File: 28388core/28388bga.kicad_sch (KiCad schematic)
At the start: 132 parts, among them IC1 F28388DZWTS, IC2 TPS62420DRCT, IC6 OPA4350EA_250, IC7 TPS3702CX33DDCT, IC8 CDCLVC1104PW, IC9 TPS3702CX12DDCT, J9 Conn_02x07_Odd_Even, Q1 FMMT618TA, Q11 AT24C16C-SSHM-T, Q2 FMMT618TA, Q4 FMMT618TA, Q46 TYPEC-304-ACP16, Q7 FMMT618TA, SW1 SW_DIP_x02, SW2 SW_Push, U1 ADR423ARMZ, Y1 ECS-2520S33-250-FN-TR

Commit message: 使用4个50PIN引脚，通常按照337封装分配位置
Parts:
- removed CN4: ~, 1mmlab_footprint:CONN-SMD_200P-P0.50_X0510WVS-200AS-LPV01, symbol 1mmlab:X0510WVS-200AS-LPV01
- added J2, J3, J4, J5: ~, 1mmlab_footprint:CONN-SMD_50P-P0.50_XKB_X0515WVS-50AS-9TV01, symbol 1mmlab:X0515WVS-50AS-9TV01
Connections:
- net GPIO44 is gone; now on net ESC_TX1_CLK: IC1.K18 (GPIO44)
- net GPIO45 is gone; now on net ESC_TX1_EN: IC1.K19 (GPIO45)
- net GPIO46 is gone; now on net ESC_MDC: IC1.E19 (GPIO46)
- net GPIO47 is gone; now on net ESC_MDIO: IC1.E18 (GPIO47)
- net GPIO63 is gone; now on net ESC_RX1_D0: IC1.J16 (GPIO63)
- net GPIO64 is gone; now on net ESC_RX1_D1: IC1.L17 (GPIO64)
- net GPIO65 is gone; now on net ESC_RX1_D2: IC1.K16 (GPIO65)
- net GPIO66 is gone; now on net ESC_RX1_D3: IC1.K17 (GPIO66)
- net GPIO68 is gone; now on net ESC_PHY1: IC1.C18 (GPIO68)
- net GPIO69 is gone; now on net ESC_RX1_CLK: IC1.B18 (GPIO69)
- net GPIO70 is gone; now on net ESC_RX1_DV: IC1.A17 (GPIO70)
- net GPIO71 is gone; now on net ESC_RX1_ERR: IC1.B17 (GPIO71)
- net GPIO72 is gone; now on net ESC_TX1_D3: IC1.B16 (GPIO72), R49.2, SW1.1
- net GPIO73 is gone; now on net ESC_TX1_D2: IC1.A16 (GPIO73)
- net GPIO74 is gone; now on net ESC_TX1_D1: IC1.C17 (GPIO74)
- net GPIO75 is gone; now on net ESC_TX1_D0: IC1.D16 (GPIO75)
- net GPIO76 is gone; now on net ESC_RESET: IC1.C16 (GPIO76)
- net GPIO77 is gone; now on net ESC_RX0_CLK: IC1.A15 (GPIO77)
- net GPIO78 is gone; now on net ESC_RX0_DV: IC1.B15 (GPIO78)
- net GPIO79 is gone; now on net ESC_RX0_ERR: IC1.C15 (GPIO79)
- net GPIO80 is gone; now on net ESC_RX0_D0: IC1.D15 (GPIO80)
- net GPIO81 is gone; now on net ESC_RX0_D1: IC1.A14 (GPIO81)
- net GPIO82 is gone; now on net ESC_RX0_D2: IC1.B14 (GPIO82)
- net GPIO83 is gone; now on net ESC_RX0_D3: IC1.C14 (GPIO83)
- net GPIO84 is gone; now on net ESC_TX0_EN: IC1.A11 (GPIO84), R47.2, SW1.2
- net GPIO85 is gone; now on net ESC_TX0_CLK: IC1.B11 (GPIO85)
- net GPIO87 is gone; now on net ESC_TX0_D0: IC1.D11 (GPIO87)
- net ADC_14_IN: now also J2.21
- net ADC_15_IN: now also J2.23
- net ADC_A0_IN: now also J2.3
- net ADC_A1_IN: now also J2.5
- net ADC_A2_IN: now also J2.9
- net ADC_A3_IN: now also J2.11
- net ADC_A4_IN: now also J2.15
- net ADC_A5_IN: now also J2.17
- net ADC_B0_IN: now also J2.4
- net ADC_B1_IN: now also J2.6
- net ADC_B2_IN: now also J2.10
- net ADC_B3_IN: now also J2.12
- net ADC_B4_IN: now also J2.16
- net ADC_B5_IN: now also J2.18
- net ADC_C2_IN: now also J2.27
- net ADC_C3_IN: now also J2.29
- net ADC_C4_IN: now also J2.33
- net ADC_C5_IN: now also J2.35
- net ADC_D0_IN: now also J2.22
- net ADC_D1_IN: now also J2.24
- net ADC_D2_IN: now also J2.28
- net ADC_D3_IN: now also J2.30
- net ADC_D4_IN: now also J2.34
- net ADC_D5_IN: now also J2.36
- net D+5V: now also J3.16, J3.2, J3.32, J3.50, J4.18, J4.2, J4.34, J4.50, J5.2, J5.26, J5.50
- net ESC_MDC: no longer IC1.D13 (GPIO152)
- net ESC_MDIO: no longer IC1.A12 (GPIO153)
- net ESC_PHY1: no longer IC1.A13 (GPIO149)
- net ESC_RESET: no longer IC1.C12 (GPIO155)
- net ESC_RX0_CLK: no longer IC1.A8 (GPIO163)
- net ESC_RX0_D0: no longer IC1.C5 (GPIO165)
- net ESC_RX0_D1: no longer IC1.D5 (GPIO166)
- net ESC_RX0_D2: no longer IC1.C4 (GPIO167)
- net ESC_RX0_D3: no longer IC1.D4 (GPIO168)
- net ESC_RX0_DV: no longer IC1.D9 (GPIO162)
- net ESC_RX0_ERR: no longer IC1.B8 (GPIO164)
- net ESC_RX1_CLK: no longer IC1.T18 (GPIO137)
- net ESC_RX1_D0: no longer IC1.N19 (GPIO139)
- net ESC_RX1_D1: no longer IC1.M19 (GPIO140)
- net ESC_RX1_D2: no longer IC1.M18 (GPIO141)
- net ESC_RX1_D3: no longer IC1.L19 (GPIO142)
- net ESC_RX1_DV: no longer IC1.T17 (GPIO136)
- net ESC_RX1_ERR: no longer IC1.T19 (GPIO138)
- net ESC_TX0_CLK: no longer IC1.B10 (GPIO157)
- net ESC_TX0_D0: no longer IC1.C10 (GPIO158)
- net ESC_TX0_EN: no longer IC1.D12 (GPIO156)
- net ESC_TX1_CLK: no longer IC1.U10 (GPIO130)
- net ESC_TX1_D0: no longer IC1.V10 (GPIO131)
- net ESC_TX1_D1: no longer IC1.W18 (GPIO132)
- net ESC_TX1_D2: no longer IC1.V18 (GPIO134)
- net ESC_TX1_D3: no longer IC1.U18 (GPIO135)
- net ESC_TX1_EN: no longer IC1.T10 (GPIO129)
- net GND: now also J2.1, J2.13, J2.14, J2.19, J2.2, J2.20, J2.25, J2.26, J2.31, J2.32, J2.37, J2.38, J2.7, J2.8, J3.1, J3.15, J3.31, J3.49, J4.1, J4.17, J4.33, J4.49, J5.1, J5.25, J5.49
- net GPIO0: now also J4.12
- net GPIO1: now also J4.14
- net GPIO10: now also J3.47
- net GPIO100: now also J3.19
- net GPIO101: now also J3.21
- net GPIO102: now also J3.23
- net GPIO103: now also J3.18
- net GPIO104: now also J3.20
- net GPIO105: now also J3.22
- net GPIO106: now also J3.4
- net GPIO107: now also J3.6
- net GPIO108: now also J3.8
- net GPIO109: now also J3.3
- net GPIO11: now also J3.43
- net GPIO110: now also J3.5
- net GPIO111: now also J3.7
- net GPIO112: now also J3.9
- net GPIO115: now also J5.33
- net GPIO116: now also J5.39
- net GPIO117: now also J5.34
- net GPIO119: now also J5.19
- net GPIO12: now also J3.45
- net GPIO120: now also J5.20
- net GPIO121: now also J5.12
- net GPIO122: now also J5.47
- net GPIO123: now also J5.48
- net GPIO124: now also J5.45
- net GPIO126: now also J5.43
- net GPIO127: now also J5.44
- net GPIO128: now also J5.46
- net GPIO13: now also J3.34
- net GPIO133: now also J4.38
- net GPIO14: now also J3.36
- net GPIO147: now also J4.32
- net GPIO15: now also J3.38
- net GPIO154: now also J4.29
- net GPIO16: now also J3.29
- net GPIO17: now also J3.33
- net GPIO18: now also J3.35
- net GPIO19: now also J3.37
- net GPIO2: now also J4.16
- net GPIO20: now also J3.28
- net GPIO21: now also J3.30
- net GPIO22: now also J3.17
- net GPIO23: now also J3.10
- net GPIO24: now also J3.12
- net GPIO25: now also J3.14
- net GPIO26: now also J3.11
- net GPIO27: now also J3.13
- net GPIO28: now also J5.35
- net GPIO29: now also J5.37
- net GPIO3: now also J4.19
- net GPIO30: now also J5.36
- net GPIO31: now also J5.38
- net GPIO32: now also J5.29
- net GPIO33: now also J5.31
- net GPIO34: now also J5.30
- net GPIO35: now also J5.32
- net GPIO36: now also J5.21
- net GPIO37: now also J5.23
- net GPIO38: now also J5.27
- net GPIO39: now also J5.22
- net GPIO4: now also J4.9
- net GPIO40: now also J5.24
- net GPIO41: now also J5.28
- net GPIO42: now also J4.35
- net GPIO43: now also J4.37
- net GPIO48: now also J5.7
- net GPIO49: now also J5.9
- net GPIO5: now also J4.11
- net GPIO50: now also J5.10
- net GPIO51: now also J5.11
- net GPIO52: now also J5.3
- net GPIO53: now also J5.4
- net GPIO54: now also J5.6
- net GPIO55: now also J5.8
- net GPIO56: now also J4.48
- net GPIO57: now also J4.47
- net GPIO58: now also J5.5
- net GPIO59: now also J4.40
- net GPIO6: now also J4.13
- net GPIO60: now also J4.41
- net GPIO61: now also J4.42
- net GPIO62: now also J4.39
- net GPIO67: now also J4.36
- net GPIO7: now also J4.15
- net GPIO8: now also J3.26
- net GPIO86: now also J4.25
- net GPIO88: now also J4.3
- net GPIO89: now also J4.5
- net GPIO9: now also J3.25
- net GPIO90: now also J4.4
- net GPIO91: now also J4.7
- net GPIO92: now also J4.6
- net GPIO93: now also J4.8
- net GPIO94: now also J4.10
- net GPIO95: now also J3.46
- net GPIO96: now also J3.44
- net GPIO97: now also J3.48
- net GPIO98: now also J3.27
- net GPIO99: now also J3.24
- new net GPIO129: IC1.T10 (GPIO129), J5.41
- new net GPIO130: IC1.U10 (GPIO130), J5.42
- new net GPIO131: IC1.V10 (GPIO131), J5.40
- new net GPIO132: IC1.W18 (GPIO132), J5.14
- new net GPIO134: IC1.V18 (GPIO134), J5.16
- new net GPIO135: IC1.U18 (GPIO135), J5.18
- new net GPIO136: IC1.T17 (GPIO136), J5.13
- new net GPIO137: IC1.T18 (GPIO137), J5.15
- new net GPIO138: IC1.T19 (GPIO138), J5.17
- new net GPIO139: IC1.N19 (GPIO139), J4.43
- new net GPIO140: IC1.M19 (GPIO140), J4.45
- new net GPIO141: IC1.M18 (GPIO141), J4.44
- new net GPIO142: IC1.L19 (GPIO142), J4.46
- new net GPIO149: IC1.A13 (GPIO149), J4.26
- new net GPIO152: IC1.D13 (GPIO152), J4.28
- new net GPIO153: IC1.A12 (GPIO153), J4.27
- new net GPIO155: IC1.C12 (GPIO155), J4.31
- new net GPIO156: IC1.D12 (GPIO156), J4.30
- new net GPIO157: IC1.B10 (GPIO157), J4.22
- new net GPIO158: IC1.C10 (GPIO158), J4.24
- new net GPIO162: IC1.D9 (GPIO162), J4.20
- new net GPIO163: IC1.A8 (GPIO163), J4.23
- new net GPIO164: IC1.B8 (GPIO164), J4.21
- new net GPIO165: IC1.C5 (GPIO165), J3.39
- new net GPIO166: IC1.D5 (GPIO166), J3.40
- new net GPIO167: IC1.C4 (GPIO167), J3.41
- new net GPIO168: IC1.D4 (GPIO168), J3.42
- no-connect marks 26 -> 28

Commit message: 1.USB修改AGND孤立 2.变化GPIO端子的线序 3.部分GPIO未连接 4.ADC用地包裹 5.添加底板project 6.添加了三个电容和两个螺丝盘 7.修改EtherCAT和boot冲突引脚
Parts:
- added C1, C2, C3: 0.1uF, Capacitor_SMD:C_0402_1005Metric, symbol Device:C_Small
- added H3, H4: MountingHole_Pad, MountingHole:MountingHole_2.2mm_M2_Pad_Via, symbol Mechanical:MountingHole_Pad
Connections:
- net AGND is gone; now on net GND: C51.2, D46.2 (A), Q46.A1B12 (GND), Q46.B1A12 (GND), R301.2, R302.1
- net +3V3D_DSP: now also C1.2, C2.2, C3.2
- net ADC_14_IN: now also J2.27; no longer J2.21
- net ADC_15_IN: now also J2.31; no longer J2.23
- net ADC_A1_IN: now also J2.7; no longer J2.5
- net ADC_A2_IN: now also J2.11; no longer J2.9
- net ADC_A3_IN: now also J2.15; no longer J2.11
- net ADC_A4_IN: now also J2.19; no longer J2.15
- net ADC_A5_IN: now also J2.23; no longer J2.17
- net ADC_B1_IN: now also J2.8; no longer J2.6
- net ADC_B2_IN: now also J2.12; no longer J2.10
- net ADC_B3_IN: now also J2.16; no longer J2.12
- net ADC_B4_IN: now also J2.20; no longer J2.16
- net ADC_B5_IN: now also J2.24; no longer J2.18
- net ADC_C2_IN: now also J2.35; no longer J2.27
- net ADC_C3_IN: now also J2.39; no longer J2.29
- net ADC_C4_IN: now also J2.43; no longer J2.33
- net ADC_C5_IN: now also J2.47; no longer J2.35
- net ADC_D0_IN: now also J2.28; no longer J2.22
- net ADC_D1_IN: now also J2.32; no longer J2.24
- net ADC_D2_IN: now also J2.36; no longer J2.28
- net ADC_D3_IN: now also J2.40; no longer J2.30
- net ADC_D4_IN: now also J2.44; no longer J2.34
- net ADC_D5_IN: now also J2.48; no longer J2.36
- net D+5V: now also J3.18, J3.34; no longer J3.16, J3.32
- net ESC_TX0_EN: now also IC1.D12 (GPIO156); no longer IC1.A11 (GPIO84), R47.2, SW1.2
- net ESC_TX1_D3: now also IC1.U18 (GPIO135); no longer IC1.B16 (GPIO72), R49.2, SW1.1
- net GND: now also J2.10, J2.17, J2.18, J2.21, J2.22, J2.29, J2.30, J2.33, J2.34, J2.41, J2.42, J2.45, J2.46, J2.49, J2.5, J2.50, J2.6, J2.9, J3.17, J3.33, C1.1, C2.1, C3.1; no longer J2.19, J2.20, J2.31, J2.32, J2.7, J2.8, J3.15, J3.31
- net GPIO0: now also J4.27; no longer J4.12
- net GPIO1: now also J4.15; no longer J4.14
- net GPIO10: now also J3.30; no longer J3.47
- net GPIO100: now also J3.25; no longer J3.19
- net GPIO101: now also J3.14; no longer J3.21
- net GPIO103: now also J3.21; no longer J3.18
- net GPIO104: now also J3.12; no longer J3.20
- net GPIO105: now also J3.15; no longer J3.22
- net GPIO106: now also J3.8; no longer J3.4
- net GPIO107: now also J3.3; no longer J3.6
- net GPIO108: now also J3.5; no longer J3.8
- net GPIO109: now also J3.4; no longer J3.3
- net GPIO11: now also J3.38; no longer J3.43
- net GPIO110: now also J3.6; no longer J3.5
- net GPIO111: no longer J3.7
- net GPIO112: no longer J3.9
- net GPIO115: now also J5.30; no longer J5.33
- net GPIO116: now also J5.46; no longer J5.39
- net GPIO117: now also J5.35; no longer J5.34
- net GPIO118: now also J5.33
- net GPIO12: now also J3.26; no longer J3.45
- net GPIO120: now also J5.21; no longer J5.20
- net GPIO121: now also J5.28; no longer J5.12
- net GPIO122: now also J5.40; no longer J5.47
- net GPIO123: now also J5.42; no longer J5.48
- net GPIO124: now also J5.38; no longer J5.45
- net GPIO125: now also J5.45
- net GPIO126: now also J5.47; no longer J5.43
- net GPIO127: now also J5.36; no longer J5.44
- net GPIO128: now also J5.48; no longer J5.46
- net GPIO13: now also J3.36; no longer J3.34
- net GPIO130: now also J5.43; no longer J5.42
- net GPIO131: now also J5.34; no longer J5.40
- net GPIO132: now also J5.22; no longer J5.14
- net GPIO133: now also J4.24; no longer J4.38
- net GPIO136: now also J5.9; no longer J5.13
- net GPIO137: now also J5.12; no longer J5.15
- net GPIO138: now also J5.10; no longer J5.17
- net GPIO139: now also J4.44; no longer J4.43
- net GPIO14: now also J3.24; no longer J3.36
- net GPIO140: now also J4.42; no longer J4.45
- net GPIO141: now also J4.36; no longer J4.44
- net GPIO142: now also J4.32; no longer J4.46
- net GPIO147: now also J4.16; no longer J4.32
- net GPIO149: now also J4.39; no longer J4.26
- net GPIO15: now also J3.43; no longer J3.38
- net GPIO152: now also J4.35; no longer J4.28
- net GPIO153: now also J4.29; no longer J4.27
- net GPIO154: now also J4.14; no longer J4.29
- net GPIO155: now also J4.45; no longer J4.31
- net GPIO157: now also J4.12; no longer J4.22
- net GPIO158: now also J4.37; no longer J4.24
- net GPIO16: now also J3.41; no longer J3.29
- net GPIO162: now also J4.21; no longer J4.20
- net GPIO163: now also J4.31; no longer J4.23
- net GPIO164: now also J4.10; no longer J4.21
- net GPIO165: now also J3.46; no longer J3.39
- net GPIO166: now also J3.28; no longer J3.40
- net GPIO167: now also J3.44; no longer J3.41
- net GPIO168: now also J3.45; no longer J3.42
- net GPIO17: now also J3.22; no longer J3.33
- net GPIO18: now also J3.37; no longer J3.35
- net GPIO19: now also J3.39; no longer J3.37
- net GPIO2: now also J4.11; no longer J4.16
- net GPIO20: now also J3.20; no longer J3.28
- net GPIO21: now also J3.31; no longer J3.30
- net GPIO22: now also J3.19; no longer J3.17
- net GPIO23: now also J3.11; no longer J3.10
- net GPIO24: now also J3.9; no longer J3.12
- net GPIO25: now also J3.10; no longer J3.14
- net GPIO26: now also J3.13; no longer J3.11
- net GPIO27: now also J3.7; no longer J3.13
- net GPIO28: now also J5.32; no longer J5.35
- net GPIO29: now also J5.44; no longer J5.37
- net GPIO3: now also J4.8; no longer J4.19
- net GPIO30: now also J5.37; no longer J5.36
- net GPIO31: now also J5.39; no longer J5.38
- net GPIO32: now also J5.31; no longer J5.29
- net GPIO33: now also J5.29; no longer J5.31
- net GPIO34: now also J5.27; no longer J5.30
- net GPIO35: now also J5.23; no longer J5.32
- net GPIO36: now also J5.20; no longer J5.21
- net GPIO37: now also J5.17; no longer J5.23
- net GPIO38: now also J5.15; no longer J5.27
- net GPIO39: now also J5.24; no longer J5.22
- net GPIO4: now also J4.23; no longer J4.9
- net GPIO40: now also J5.18; no longer J5.24
- net GPIO41: now also J5.13; no longer J5.28
- net GPIO42: now also J4.20; no longer J4.35
- net GPIO43: now also J4.47; no longer J4.37
- net GPIO48: now also J5.11; no longer J5.7
- net GPIO49: now also J5.5; no longer J5.9
- net GPIO5: now also J4.7; no longer J4.11
- net GPIO50: now also J5.8; no longer J5.10
- net GPIO51: now also J5.6; no longer J5.11
- net GPIO52: now also J5.7; no longer J5.3
- net GPIO53: now also J4.48; no longer J5.4
- net GPIO54: now also J5.4; no longer J5.6
- net GPIO55: now also J5.3; no longer J5.8
- net GPIO56: now also J4.40; no longer J4.48
- net GPIO57: now also J4.46; no longer J4.47
- net GPIO58: now also J4.38; no longer J5.5
- net GPIO59: now also J4.28; no longer J4.40
- net GPIO6: now also J4.19; no longer J4.13
- net GPIO60: now also J4.30; no longer J4.41
- net GPIO61: now also J4.26; no longer J4.42
- net GPIO62: now also J4.22; no longer J4.39
- net GPIO67: now also J4.43; no longer J4.36
- net GPIO7: now also J4.6; no longer J4.15
- net GPIO8: now also J3.16; no longer J3.26
- net GPIO86: now also J4.41; no longer J4.25
- net GPIO88: now also J4.13; no longer J4.3
- net GPIO89: now also J4.3; no longer J4.5
- net GPIO9: now also J3.27; no longer J3.25
- net GPIO90: now also J4.9; no longer J4.4
- net GPIO91: now also J4.4; no longer J4.7
- net GPIO92: now also J4.5; no longer J4.6
- net GPIO93: now also J3.48; no longer J4.8
- net GPIO94: now also J3.42; no longer J4.10
- net GPIO95: now also J3.32; no longer J3.46
- net GPIO96: now also J3.47; no longer J3.44
- net GPIO97: now also J3.40; no longer J3.48
- net GPIO98: now also J3.35; no longer J3.27
- net GPIO99: now also J3.29; no longer J3.24
- net PE_GND: now also H3.1, H4.1
- net unconnected-(Q46-PadEP)_1: now reaches Q46.EP
- removed net GPIO135: IC1.U18 (GPIO135), J5.18
- removed net GPIO156: IC1.D12 (GPIO156), J4.30
- new net GPIO72: IC1.B16 (GPIO72), J5.14, R49.2, SW1.1
- new net GPIO84: IC1.A11 (GPIO84), J4.25, R47.2, SW1.2
- no-connect marks 28 -> 16
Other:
- note added: "新增2个螺丝孔盘"
- note added: "新增3个电容"

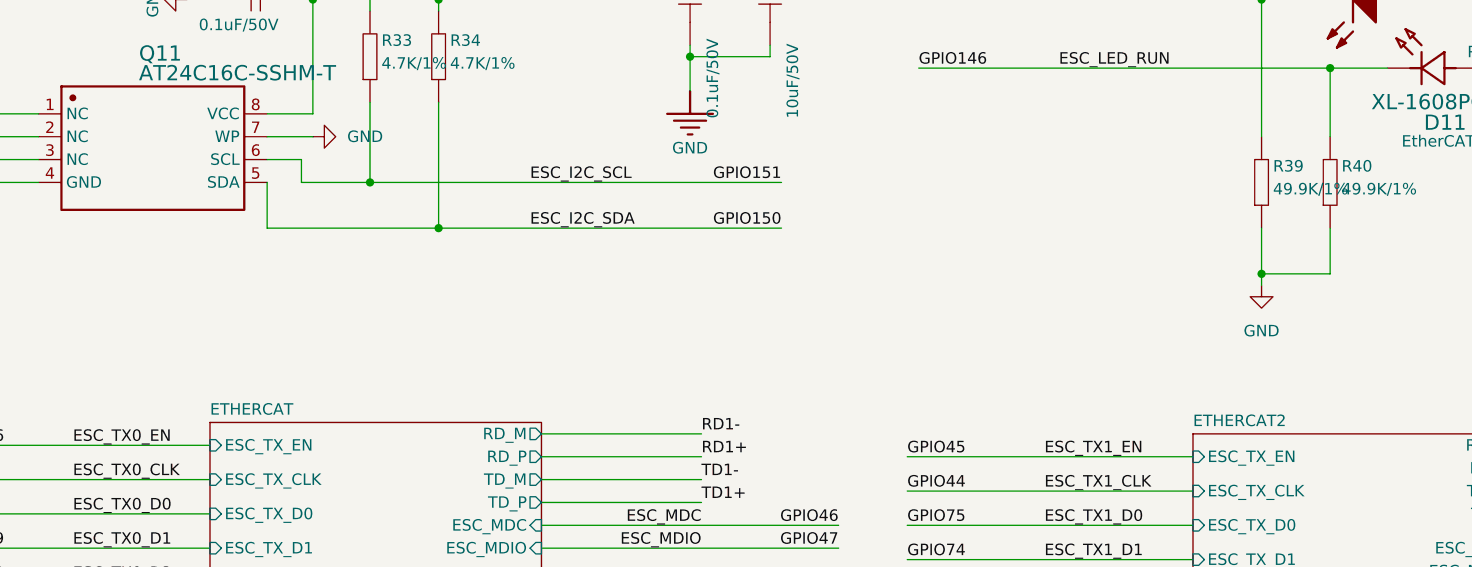
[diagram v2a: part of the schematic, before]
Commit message: 底板分配引脚
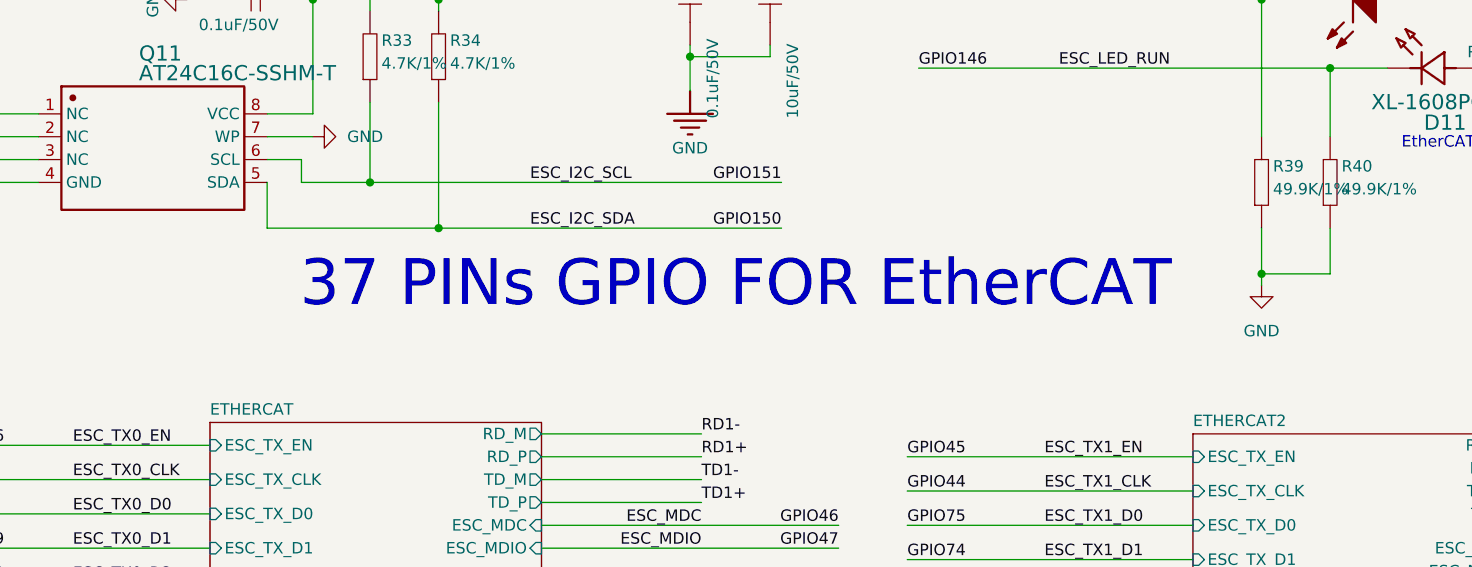
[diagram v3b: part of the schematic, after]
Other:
- note added: "37 PINs GPIO FOR EtherCAT"
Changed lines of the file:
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@@
+		)
+	)
+	(text "37 PINs GPIO FOR EtherCAT\n\n"
+		(exclude_from_sim no)
+		(at 257.81 269.494 0)
+		(effects
+			(font
+				(size 5.08 5.08)
+			)
 		)
 	)

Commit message: 核心板布线完成
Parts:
- J2, J3, J4, J5: JLC_3DModel_Q (none) -> e98c08ee72e142efab7a86d5099c10a0; JLC_3D_Size (none) -> 15.2 5.2
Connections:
- net ADC_14: now also IC1.U4 (ADCIN15_CMPIN4N); no longer IC1.T4 (ADCIN14_CMPIN4P)
- net ADC_15: now also IC1.U1 (ADCINA0_DACOUTA); no longer IC1.U4 (ADCIN15_CMPIN4N)
- net ADC_A0: now also IC1.U7 (ADCIND5); no longer IC1.U1 (ADCINA0_DACOUTA)
- net ADC_A1: now also IC1.U5 (ADCIND1_CMPIN7N); no longer IC1.T1 (ADCINA1_DACOUTB)
- net ADC_A2: now also IC1.W4 (ADCINB5); no longer IC1.U2 (ADCINA2_CMPIN1P)
- net ADC_A3: now also IC1.W3 (ADCINB3_CMPIN3N); no longer IC1.T2 (ADCINA3_CMPIN1N)
- net ADC_A4: now also IC1.W2 (ADCINB1_DACOUTC); no longer IC1.U3 (ADCINA4_CMPIN2P)
- net ADC_A5: now also IC1.T5 (ADCIND0_CMPIN7P); no longer IC1.T3 (ADCINA5_CMPIN2N)
- net ADC_B0: now also IC1.T7 (ADCIND4); no longer IC1.V2 (ADCINB0_VDAC)
- net ADC_B1: now also IC1.U6 (ADCIND3_CMPIN8N); no longer IC1.W2 (ADCINB1_DACOUTC)
- net ADC_B2: now also IC1.T6 (ADCIND2_CMPIN8P); no longer IC1.V3 (ADCINB2_CMPIN3P)
- net ADC_B3: now also IC1.V4 (ADCINB4); no longer IC1.W3 (ADCINB3_CMPIN3N)
- net ADC_B4: now also IC1.V3 (ADCINB2_CMPIN3P); no longer IC1.V4 (ADCINB4)
- net ADC_B5: now also IC1.V2 (ADCINB0_VDAC); no longer IC1.W4 (ADCINB5)
- net ADC_C2: now also IC1.T3 (ADCINA5_CMPIN2N); no longer IC1.R3 (ADCINC2_CMPIN6P)
- net ADC_C3: now also IC1.T1 (ADCINA1_DACOUTB); no longer IC1.P3 (ADCINC3_CMPIN6N)
- net ADC_D0: now also IC1.U3 (ADCINA4_CMPIN2P); no longer IC1.T5 (ADCIND0_CMPIN7P)
- net ADC_D1: now also IC1.U2 (ADCINA2_CMPIN1P); no longer IC1.U5 (ADCIND1_CMPIN7N)
- net ADC_D2: now also IC1.T4 (ADCIN14_CMPIN4P); no longer IC1.T6 (ADCIND2_CMPIN8P)
- net ADC_D3: now also IC1.T2 (ADCINA3_CMPIN1N); no longer IC1.U6 (ADCIND3_CMPIN8N)
- net ADC_D4: now also IC1.R3 (ADCINC2_CMPIN6P); no longer IC1.T7 (ADCIND4)
- net ADC_D5: now also IC1.P3 (ADCINC3_CMPIN6N); no longer IC1.U7 (ADCIND5)
- net GPIO107: no longer R108.2
- net GPIO111: now also R12.2
- net GPIO112: now also R17.2
- net GPIO113: now also R1.2; no longer R17.2
- net GPIO114: now also R5.2; no longer R12.2
- net GPIO118: no longer R5.2
- net GPIO125: no longer R1.2
- net GPIO137: now also J5.10; no longer J5.12
- net GPIO138: now also J5.14; no longer J5.10
- net GPIO4: now also J4.19; no longer J4.23
- net GPIO51: now also J5.12; no longer J5.6
- net GPIO54: now also J5.6; no longer J5.4
- net GPIO57: now also J5.4; no longer J4.46
- net GPIO6: now also J4.23; no longer J4.19
- net GPIO62: now also R108.2; no longer J4.22
- net GPIO72: no longer J5.14
- net GPIO84: no longer J4.25
- net unconnected-(Q46-PadEP)_1: no longer names the net of Q46.EP
- no-connect marks 16 -> 19
